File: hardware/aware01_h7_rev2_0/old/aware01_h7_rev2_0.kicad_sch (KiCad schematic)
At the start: 14 parts, among them J2 Conn_02x07_Odd_Even, SW1 SW_Push, U2 STM32H7A3RITx, Y2 WE-XTAL 24.0MHz 50ppm

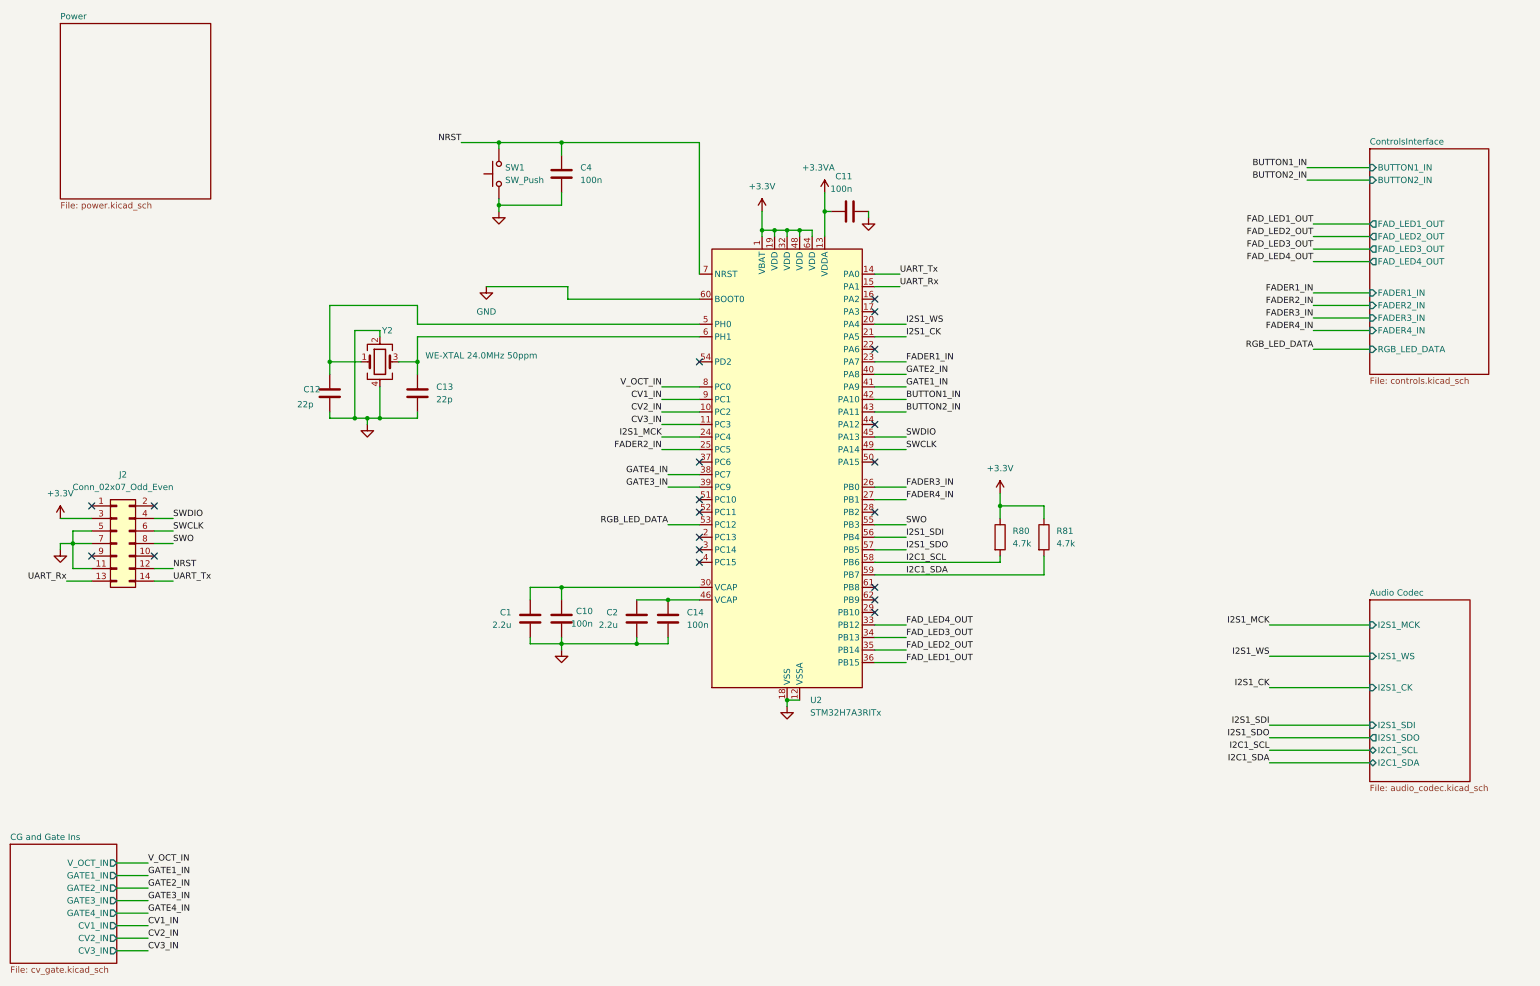
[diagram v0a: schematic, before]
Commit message: add 5V buck converter
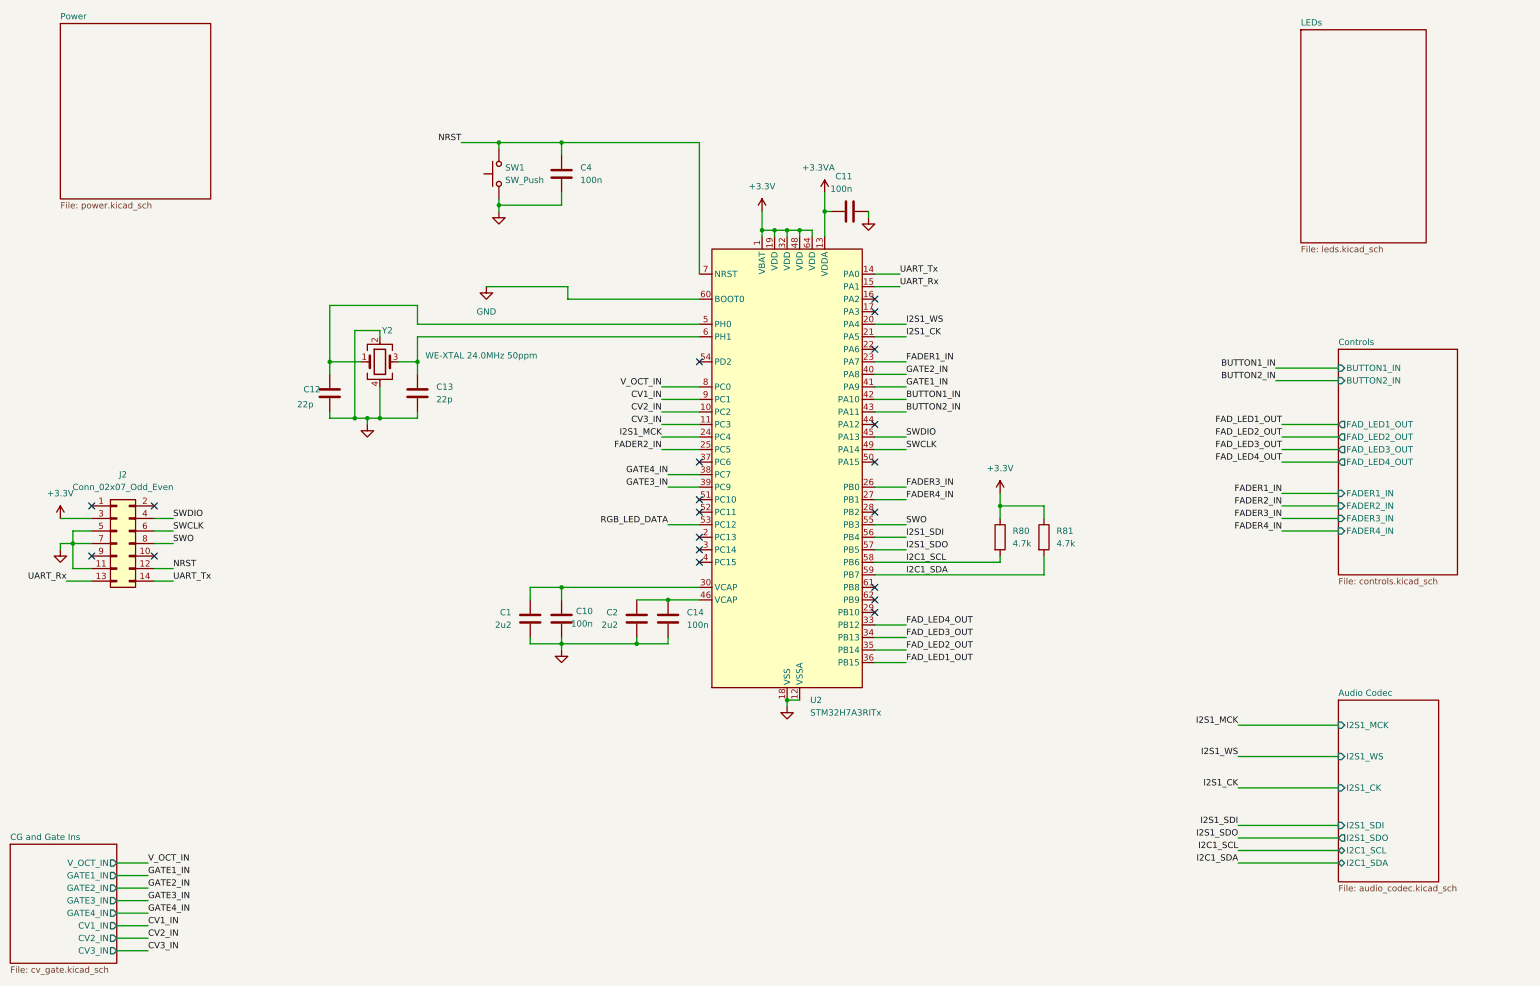
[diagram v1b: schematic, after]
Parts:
- C1, C2: value 2.2u -> 2u2; Manufacturer_Name TAIYO YUDEN -> (none); Manufacturer_Part_Number TMK107ABJ225KA-T -> (none); Mouser Part Number 963-TMK107ABJ225KA-T -> (none)
- J2: Manufacturer_Name Harwin -> (none); Manufacturer_Part_Number M50-3500742 -> (none); Mouser Part Number 855-M50-3500742 -> (none)
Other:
- sheet ControlsInterface renamed Controls
- added sheet LEDs (leds.kicad_sch)
- sheet Controls ports: added none; removed RGB_LED_DATA
